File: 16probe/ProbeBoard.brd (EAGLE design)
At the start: 54 x 13 mm, 60 parts, among them Q1 2N7002, Q2 2N7002, U1 LTC2495CUHFPBF, U3 MAX6037AAUKADJ+T, U4 CSTCE16M0V53A-R0, U5 TPS79733DCKR, U6 ATMEGA328P_TQFPQFN_32

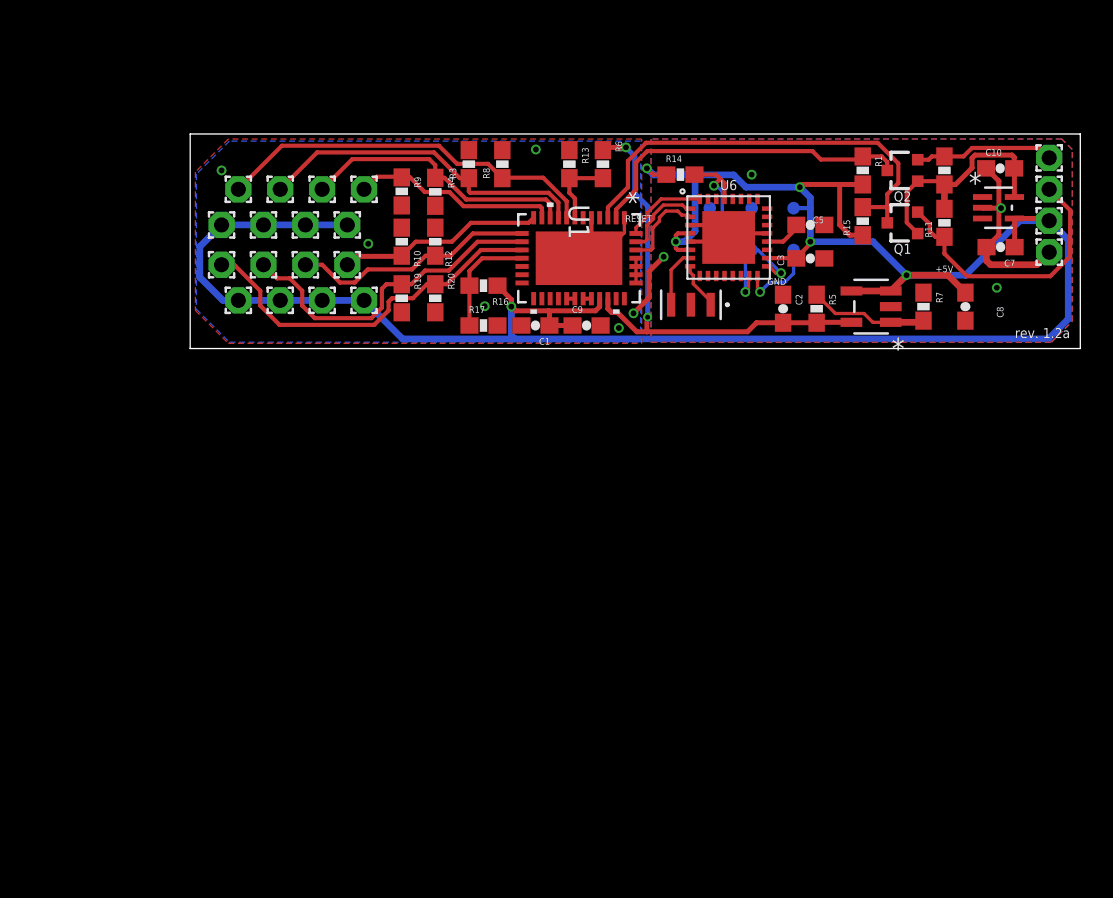
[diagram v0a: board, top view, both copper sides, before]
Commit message: begin 16 probe layout
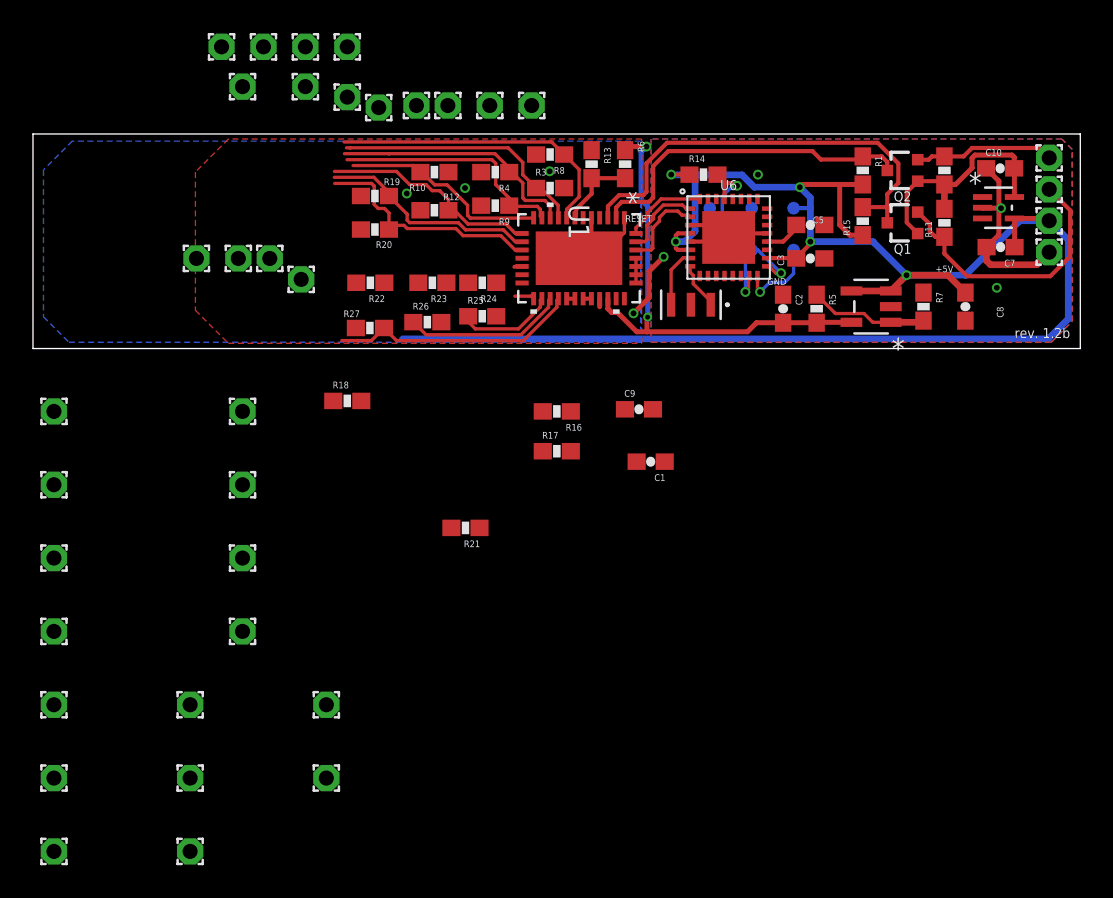
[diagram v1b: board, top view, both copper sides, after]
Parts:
- added R18, R21, R22, R23, R24, R25, R26, R27: 2.2k, SparkFun:0603-RES
- added TEMP1-5V1, TEMP10, TEMP11, TEMP12, TEMP13, TEMP14, TEMP15, TEMP16, TEMP2-5V1, TEMP3-5V1, TEMP4-5V1, TEMP5-5V1, TEMP6-5V1, TEMP7-5V1, TEMP8-5V1, TEMP9: (no value), wirepad:1,6/0,9
- moved TEMP1 18.5 mm to (30.2, 14.7)
- moved TEMP2 13.7 mm to (27.7, 14.7)
- moved TEMP7 11.1 mm to (16.5, 15.9)
- moved TEMP8 10.9 mm to (12.7, 15.9)
- moved C1 10.8 mm to (37.4, -6.86)
- moved TEMP1-5V 10.8 mm to (16.5, 18.3)
- moved TEMP4-5V 10.8 mm to (11.4, 18.3)
- moved TEMP6-5V 10.8 mm to (14.0, 18.3)
- moved TEMP7-5V 10.8 mm to (19.1, 18.3)
- moved TEMP6 10.5 mm to (19.1, 15.2)
- moved TEMP5 9.71 mm to (21.0, 14.6)
- moved TEMP3 9.16 mm to (25.1, 14.7)
- moved R16 8.82 mm to (31.8, -3.81)
- moved R17 8.82 mm to (31.8, -6.22)
- moved R19 6.41 mm to (20.7, 9.25), turned to 180 degrees
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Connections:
- new net CH10: R22.1, TEMP11.1, U1.18
- new net CH11: R23.1, TEMP12.1, U1.19
- new net CH12: R24.1, TEMP13.1, U1.20
- new net CH13: R25.1, TEMP14.1, U1.21
- new net CH14: R26.1, TEMP15.1, U1.22
- new net CH15: R27.1, TEMP16.1, U1.23
- new net CH8: R18.1, TEMP9.1
- new net CH9: R21.1, TEMP10.1, U1.17
- net +5V: now also TEMP1-5V1.1, TEMP2-5V1.1, TEMP3-5V1.1, TEMP4-5V1.1, TEMP5-5V1.1, TEMP6-5V1.1, TEMP7-5V1.1, TEMP8-5V1.1
- net COM: now also R18.2, R21.2, R22.2, R23.2, R24.2, R25.2, R26.2, R27.2
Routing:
- net +5V: track 147.2 -> 108.6 mm, vias 6 -> 5
- net CH15: track 0.00 -> 15.1 mm
- net CH14: track 0.00 -> 9.76 mm
- net CH7: track 22.5 -> 14.5 mm
- net CH6: track 20.6 -> 13.3 mm
- net VCC_READ: track 6.82 -> 0.00 mm
- net CH13: track 0.00 -> 5.97 mm
- net CH0: track 23.4 -> 18.2 mm
- net CH1: track 20.4 -> 15.5 mm
- net CH3: track 12.5 -> 14.5 mm
- net CH2: track 17.0 -> 15.2 mm
- net CH5: track 14.8 -> 13.3 mm
- net CH12: track 0.00 -> 1.20 mm
- net RESET: track 8.11 -> 7.21 mm
- net CH9: track 0.00 -> 0.50 mm
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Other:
- board size 54 x 13 mm -> 63.5 x 13 mm
- board text added: "rev. 1.2b"
- board text removed: "0"
- board text removed: "1"
- board text removed: "2"
- board text removed: "3"
- board text removed: "4"
- board text removed: "5"
- board text removed: "6"
- board text removed: "7"
- board text removed: "rev. 1.2a"
